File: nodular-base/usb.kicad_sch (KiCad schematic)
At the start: 45 parts, among them J10 Conn_01x02_MountingPin, J7 USB_C_Receptacle_USB2.0, J8 USB_C_Receptacle_USB2.0, U2 FUSB302BMPX, U29 RCLAMP0524P-ES, U3 BQ25895RTW, U43 TLV62595DMQR, U5 FUSB302BMPX, U50 TS3USB221A, U8 MT9700

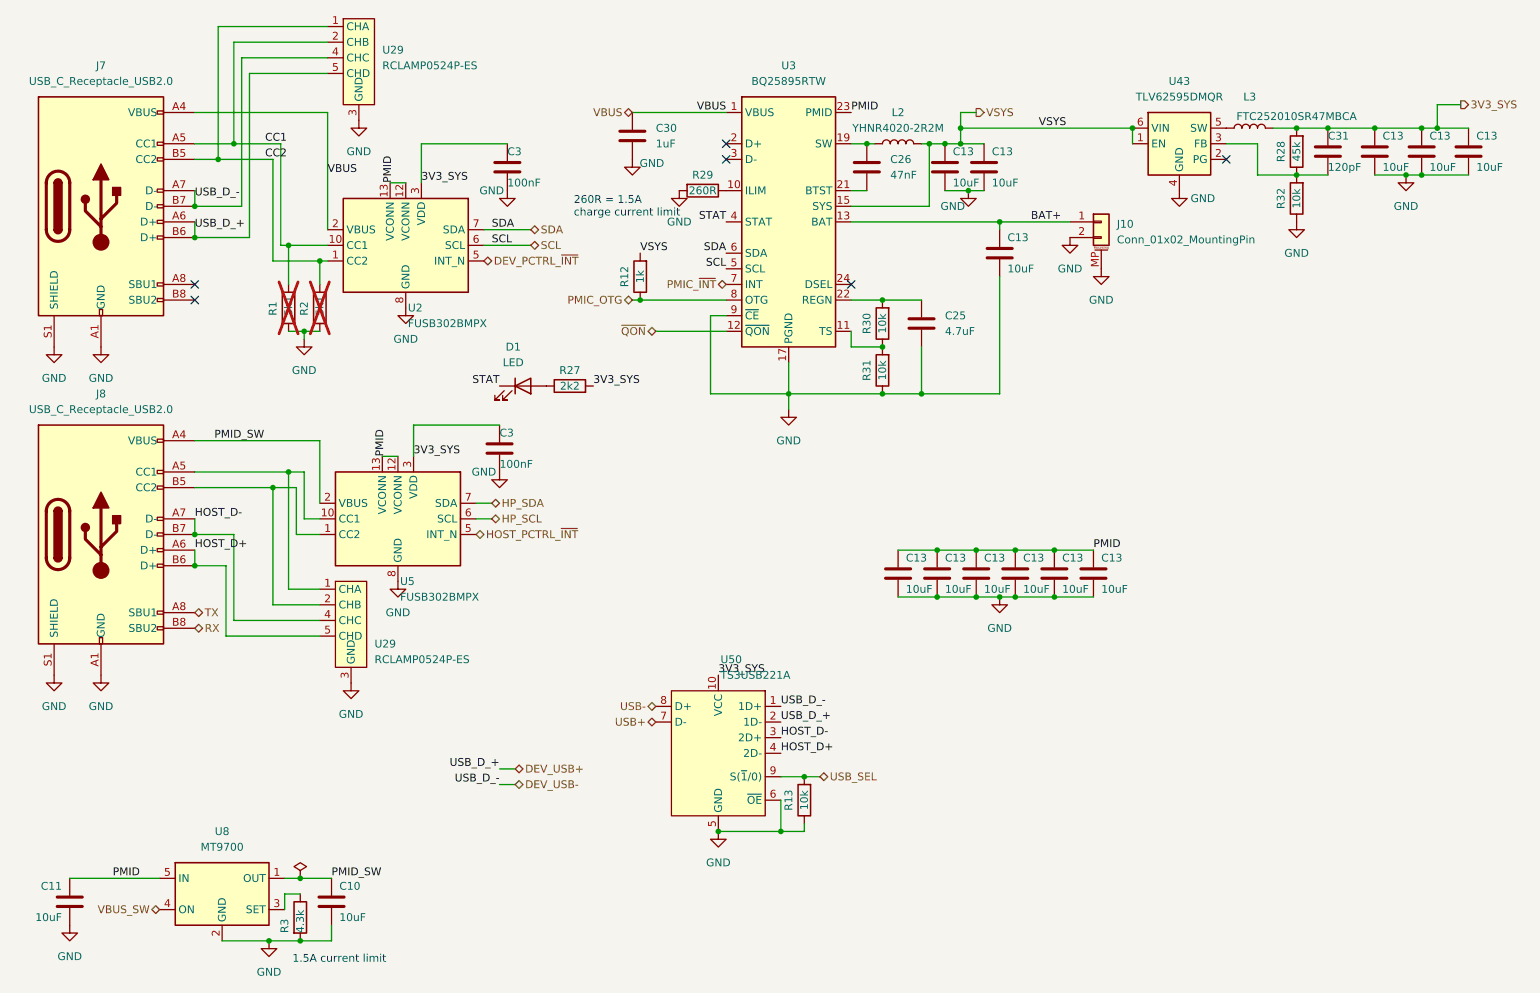
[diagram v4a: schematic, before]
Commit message: Add 3d models and fix erc errors
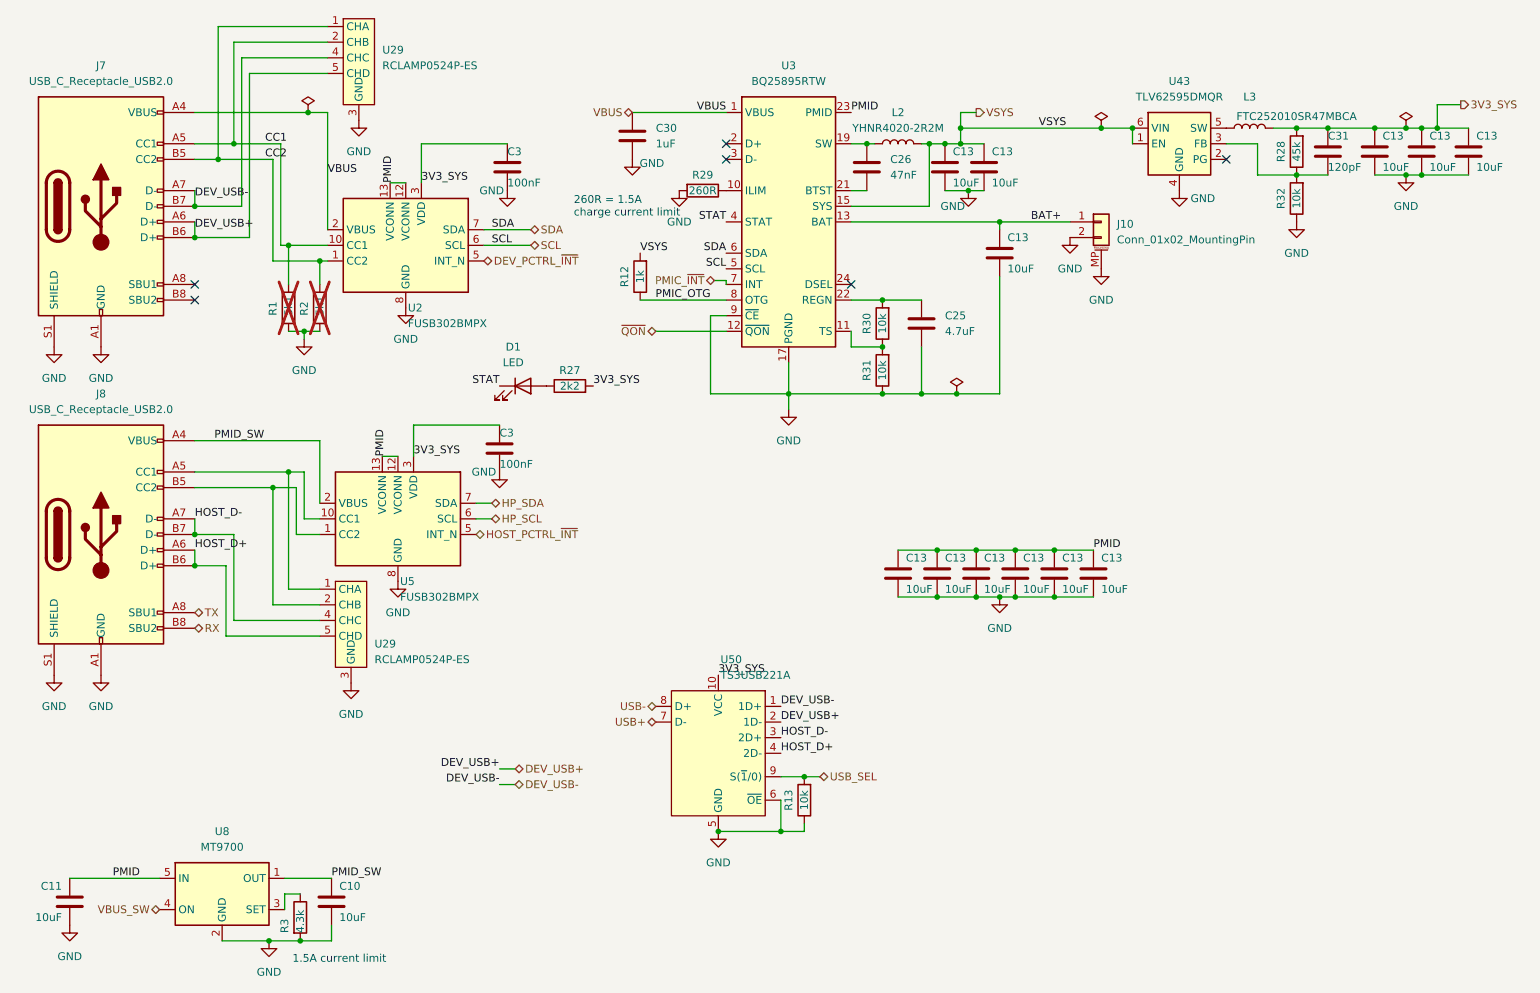
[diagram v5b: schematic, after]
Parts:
- U29: footprint Package_DFN_QFN:Diodes_UDFN-10_1.0x2.5mm_P0.5mm -> nodular:Diodes_UDFN-10_1.0x2.5mm_P0.5mm

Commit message: Add additional accelerometer-gyro option, update pin and address map, fix some ERC errors
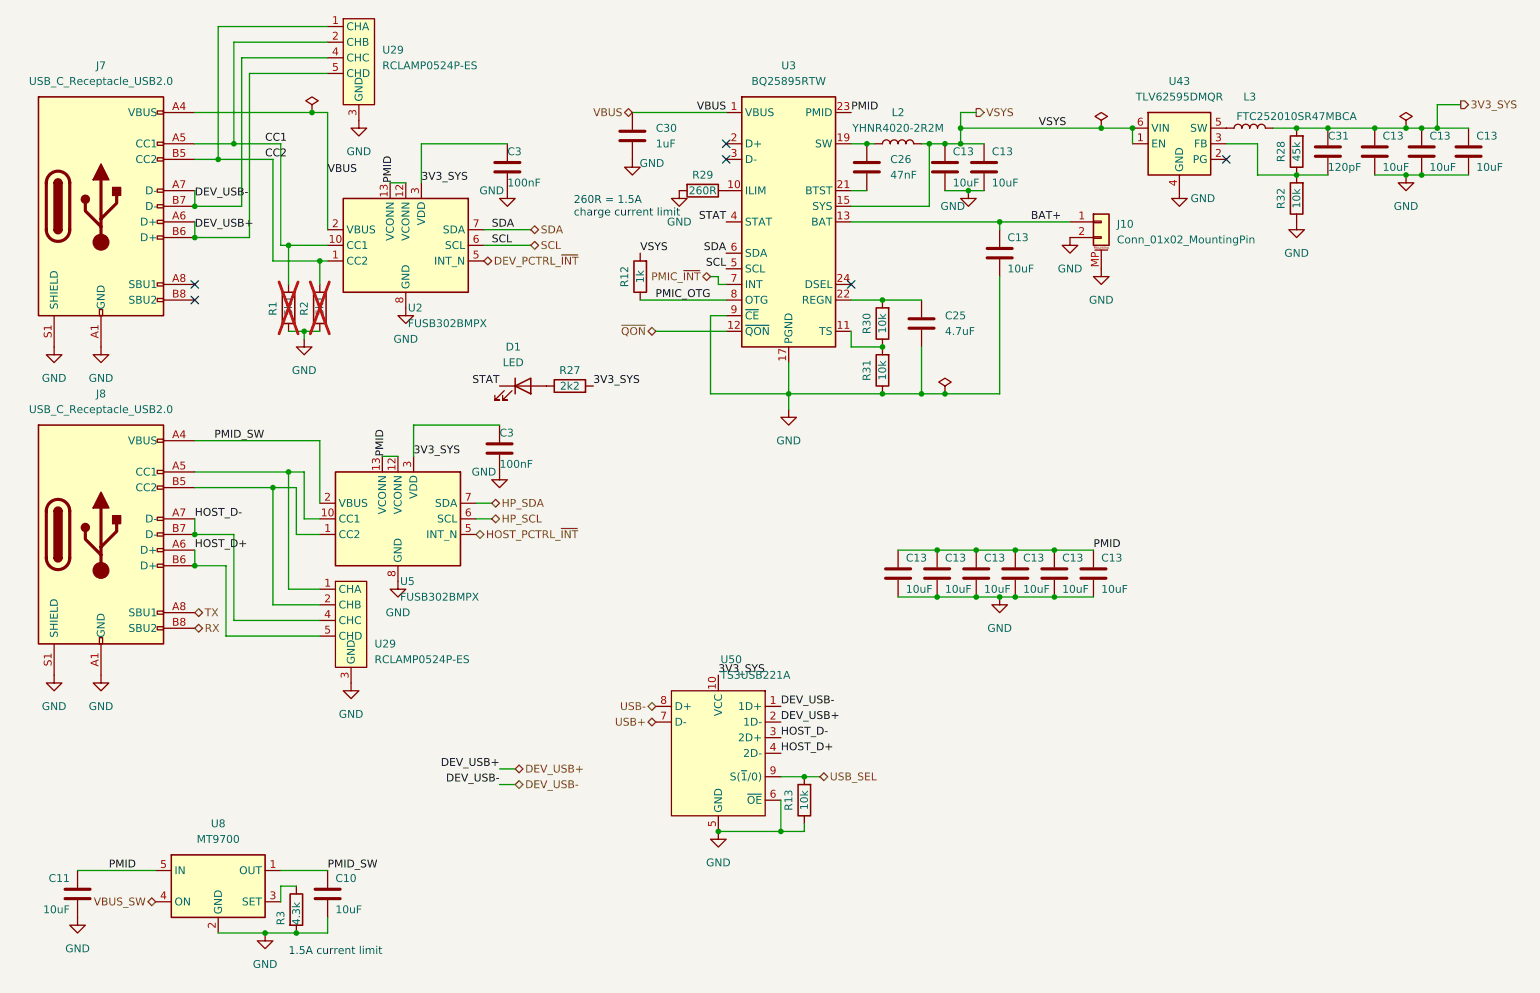
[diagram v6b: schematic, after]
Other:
- moved on the sheet: C10, C11, R3, U8

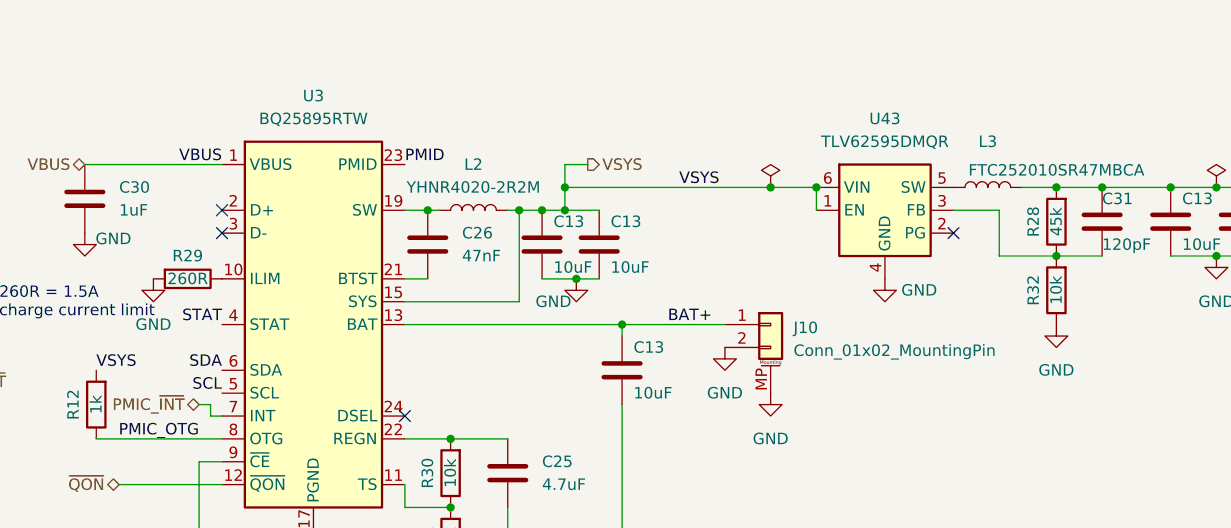
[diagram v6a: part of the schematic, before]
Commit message: Add baseline art (bart), add stencil alignment holes, complete BOM, prepare for proto order
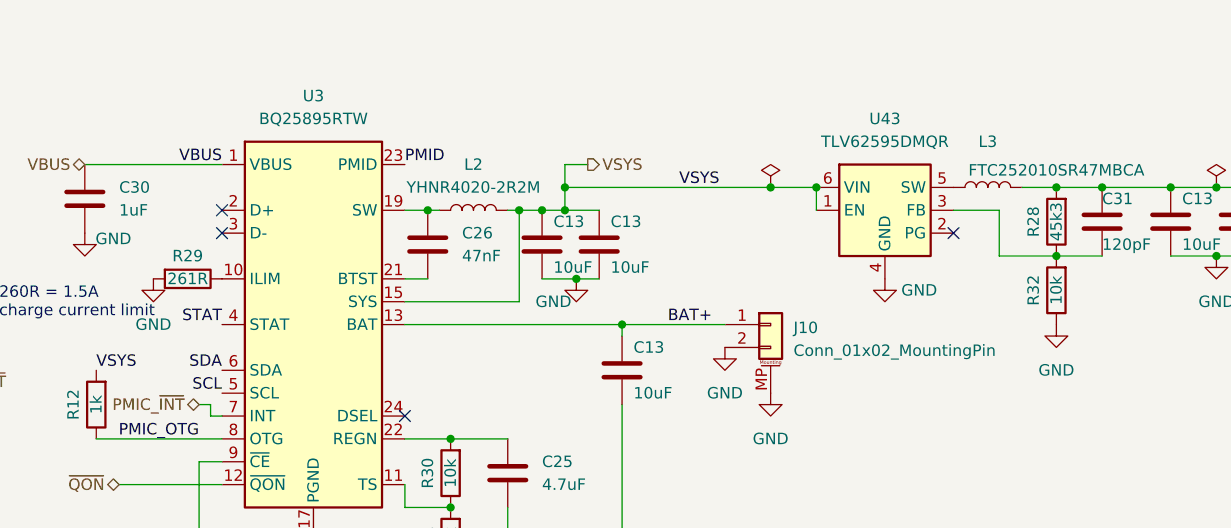
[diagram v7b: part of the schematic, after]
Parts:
- R28: value 45k -> 45k3
- R29: value 260R -> 261R
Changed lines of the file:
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@@
       (effects (font (size 1.27 1.27)))
     )
-    (property "Value" "260R" (at 140.97 46.99 90)
+    (property "Value" "261R" (at 140.97 46.99 90)
       (effects (font (size 1.27 1.27)))
     )
@@
       (effects (font (size 1.27 1.27)))
     )
-    (property "Value" "45k" (at 237.49 40.64 90)
-      (effects (font (size 1.27 1.27)))
-    )
+    (property "Value" "45k3" (at 237.49 40.64 90)
+      (effects (font (size 1.27 1.27)))
+    )

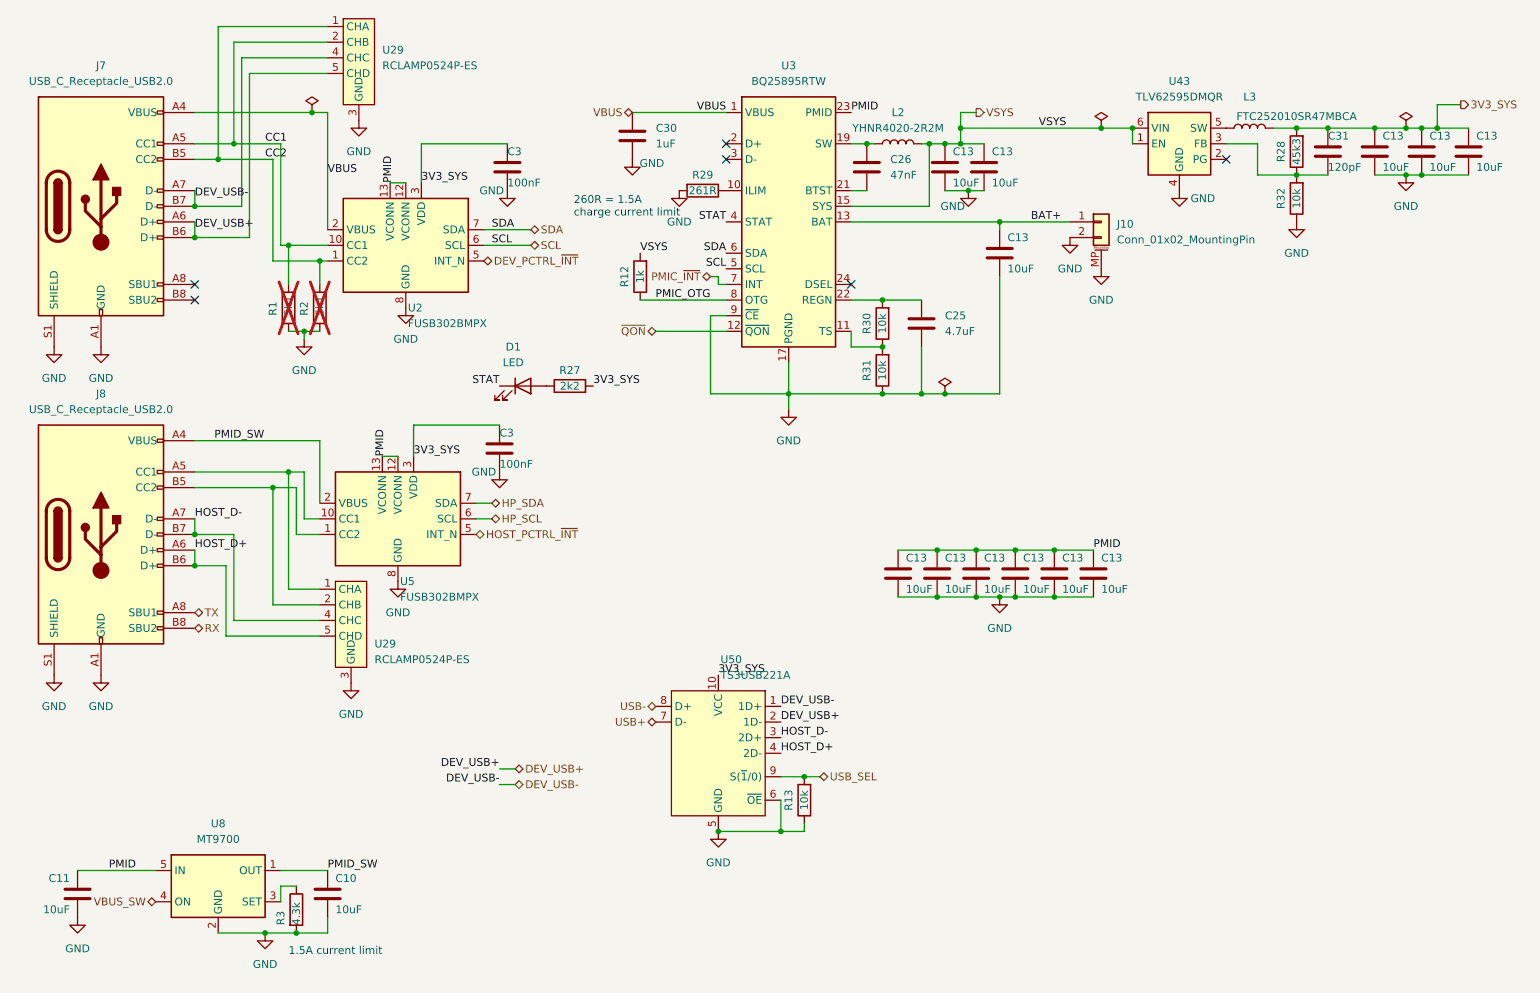
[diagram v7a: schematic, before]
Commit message: Modify base board: - Fix ESP32 strapping pins state - Remove 3/6 M3 standoffs - Change to LGA-style pads on ESP32 - Modify SFP mechanical pads to not be plated - Add larger mechanical pads with more solder paste surface to USB-C connectors
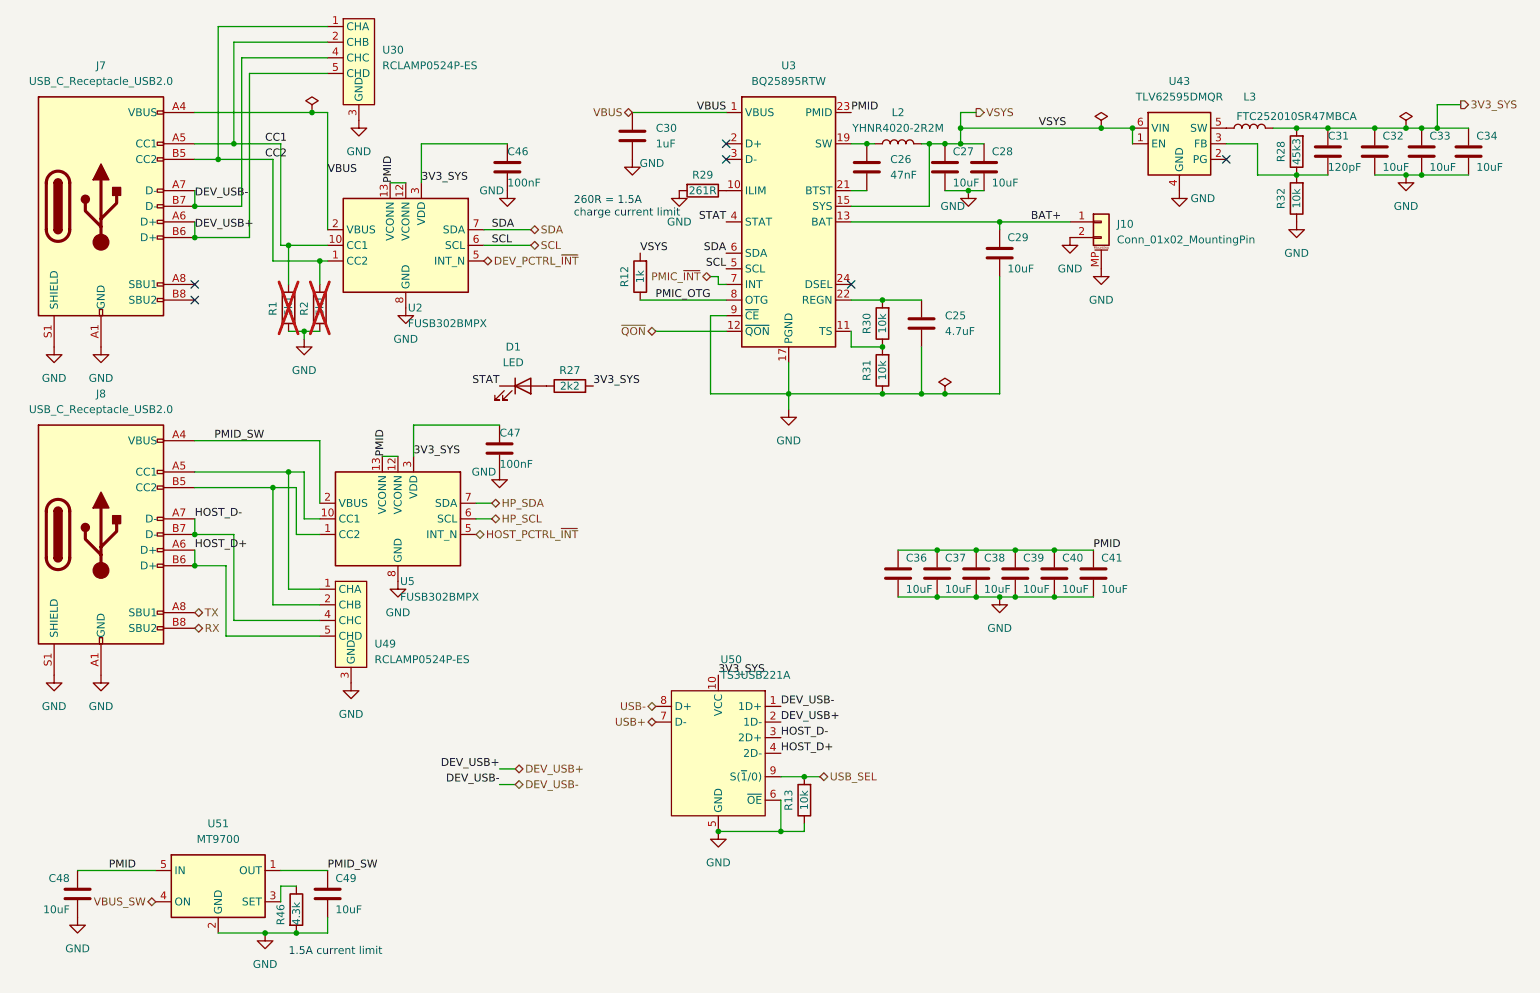
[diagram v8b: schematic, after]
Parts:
- renumbered C13 to C27, C13 to C28, C13 to C29, C13 to C32, C13 to C33, C13 to C34, C13 to C36, C13 to C37, C13 to C38, C13 to C39, C13 to C40, C13 to C41, C3 to C46, C3 to C47, C11 to C48, C10 to C49, R3 to R46, U29 to U30, U29 to U49, U8 to U51
